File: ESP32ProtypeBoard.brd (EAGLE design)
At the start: 54.6 x 53.3 mm, 102 parts, among them IC2 SI4431BDY, J1 CONN_03_NO_SILK, J2 CONN_04_NO_SILK, J20 CONN_04_NO_SILK, J21 CONN_05_NO_SILK, J24 CONN_04_NO_SILK, J31 CONN_01_NO_SILK, J38 CONN_01_NO_SILK, J4 VCC_TERMINAL, J40 CONN_01_NO_SILK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

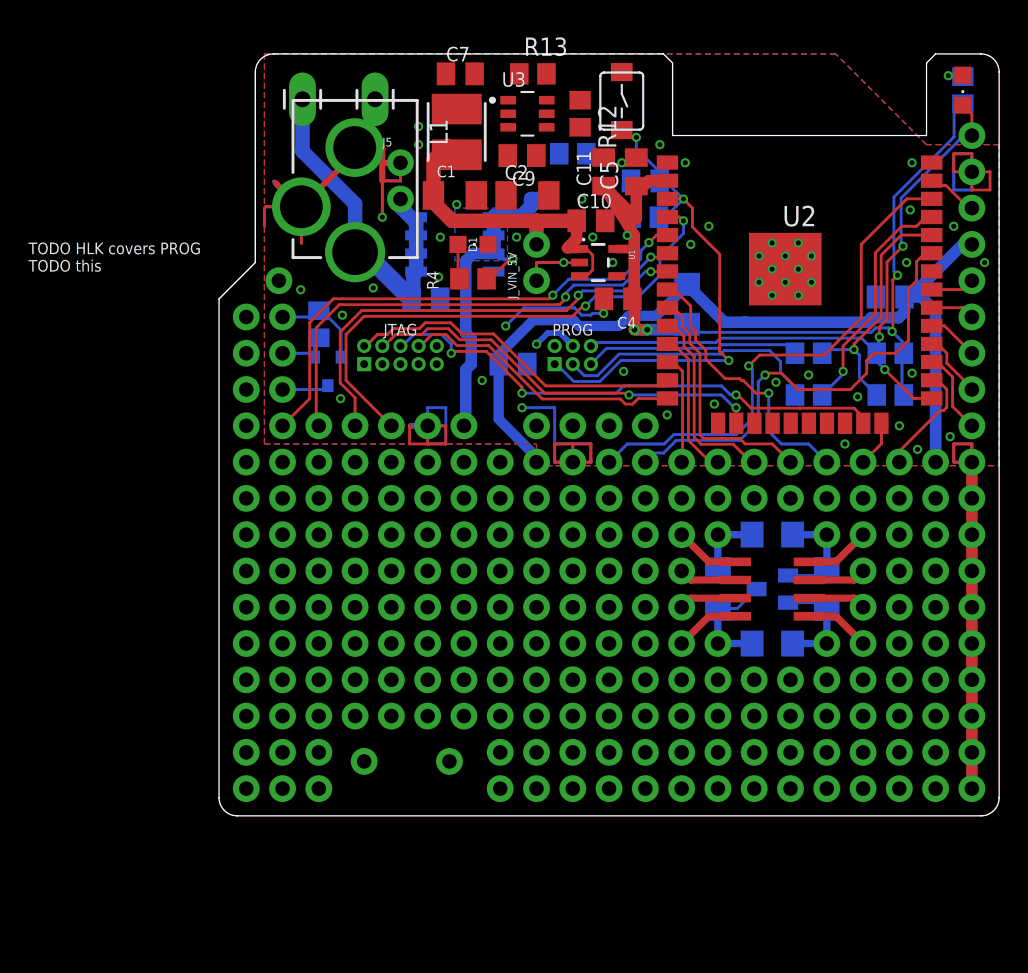
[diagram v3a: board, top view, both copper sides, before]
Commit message: Added custom modified DC-044 power jack
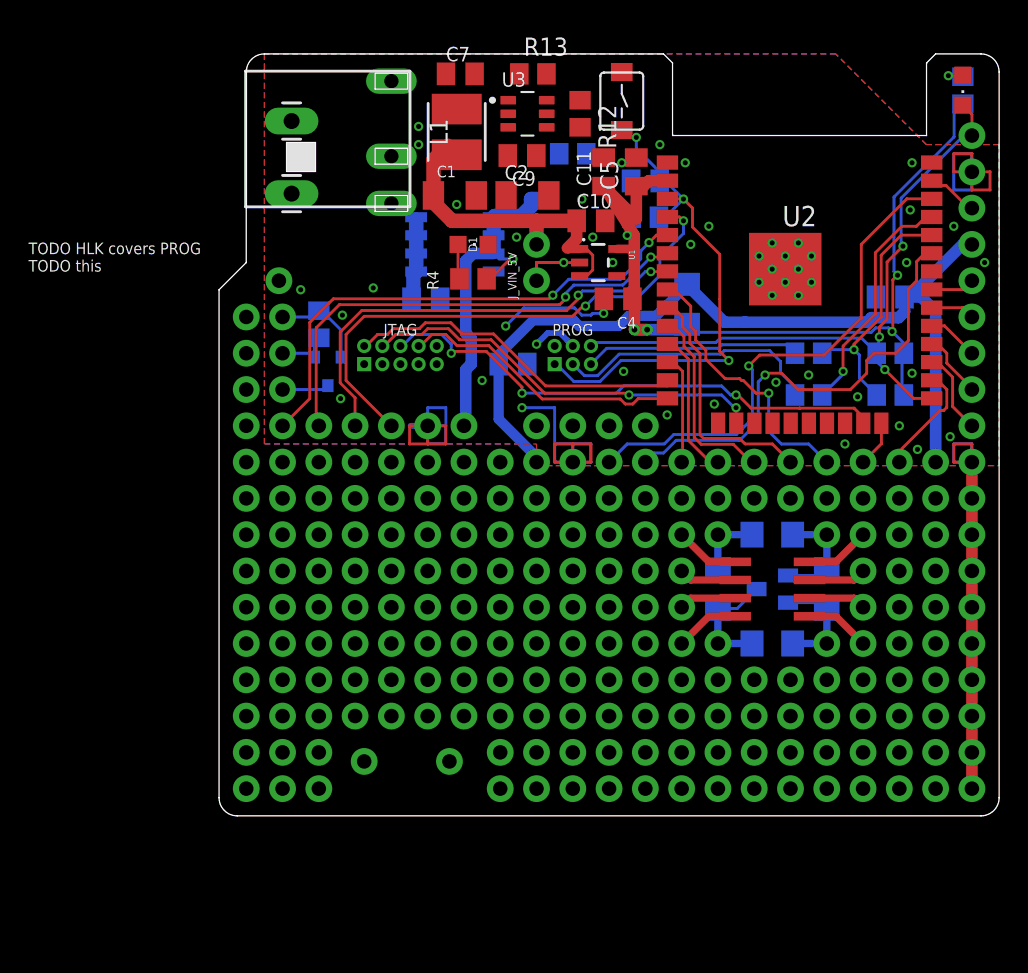
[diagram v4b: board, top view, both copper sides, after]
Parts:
- removed J37, J5: (no value), SparkFun-Connectors:1X01NS_KIT
- J10: value (none) -> DC-0440-2.5A-2.0; device SparkFun-Connectors:POWER_JACK_PTH_LOCK -> DC-0440-2.5A-2.0:DC044025A20
- moved J4 6.65 mm to (5.08, 43.6), turned to 90 degrees
- moved J3 6.04 mm to (5.08, 48.6), turned to 90 degrees
- moved J10 3.18 mm to (12.1, 51.4), turned to 0 degrees
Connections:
- net GND: now also J10.2, J10.3; no longer J10.GND, J10.GNDBREAK, J5.1
- net VCC: now also J10.1; no longer J10.PWR, J37.1
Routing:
- net GND: track 153.8 -> 111.1 mm, vias 41 -> 38
- net VCC: track 25.5 -> 5.85 mm
- removed copper zone on layer 16, net +12V
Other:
- outline, holes or cut-outs redrawn
- board text added: "7-17V"
- board text removed: "7-24V"

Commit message: WIP: new layout
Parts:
- moved C8 9.62 mm to (5.59, 39.9), flipped to the top
- moved IC2 5.18 mm to (11.4, 39.0), flipped to the top, turned to 180 degrees
- moved D1 0.51 mm to (18.3, 40.0)
- moved R4 0.51 mm to (18.3, 37.6)
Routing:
- net +12V: track 25.0 -> 13.9 mm, vias 1 -> 0
- net VCC: track 5.85 -> 2.54 mm
- net +5V: track 24.2 -> 21.2 mm
- net GND: vias 38 -> 34
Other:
- board text added: "Mikee © 2021/06 v3.1"
- board text removed: "Mikee © 2021/05 v3.1"
- board text removed: "TYA40124R7"

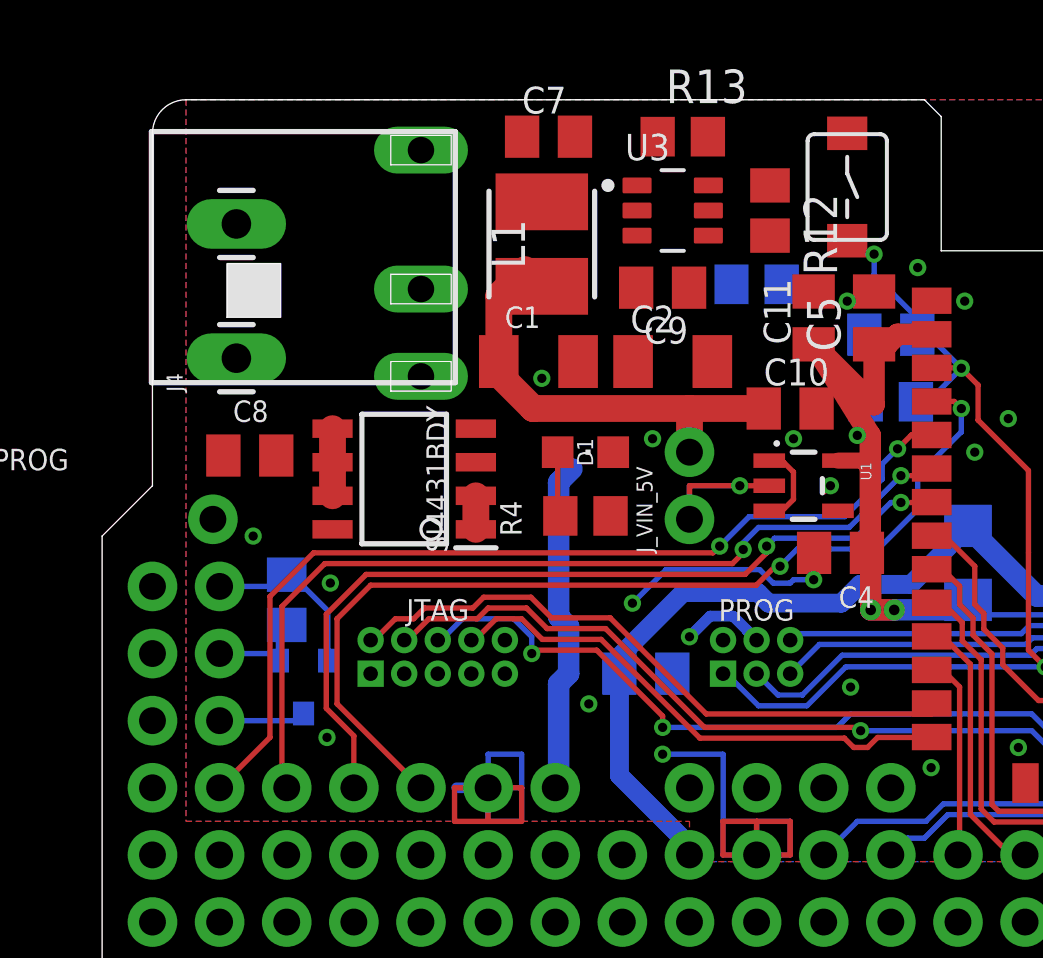
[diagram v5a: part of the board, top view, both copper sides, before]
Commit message: Wired new DCDC converter
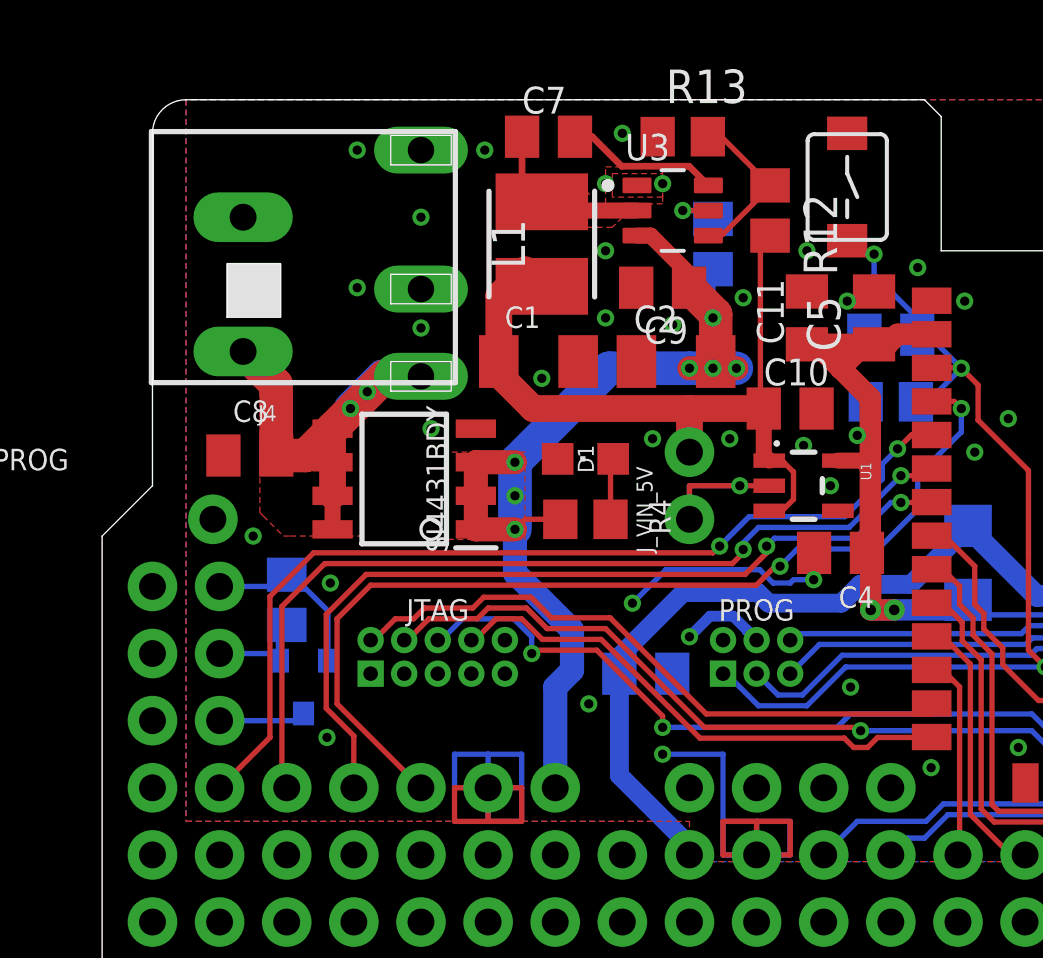
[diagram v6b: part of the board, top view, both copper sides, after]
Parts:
- J3: value (none) -> CONN_01_NO_SILK_LONGPAD; device SparkFun-Connectors:1X01_LONGPAD -> my-connectors:1X01_NO_SILK_LONGPAD
- J4: device SparkFun-Connectors:1X01_LONGPAD -> my-connectors:1X01_NO_SILK_LONGPAD
- moved R3 2.25 mm to (23.1, 47.9), turned to 90 degrees
- moved J3 0.36 mm to (5.33, 48.9), turned to 180 degrees
- moved J4 0.36 mm to (5.33, 43.8), turned to 180 degrees
- moved D1 0.25 mm to (18.3, 39.8), turned to 90 degrees
- moved C11 0.25 mm to (26.7, 45.1)
- moved C2 0.13 mm to (21.7, 43.4)
- moved R4 0.13 mm to (18.3, 37.5), turned to 0 degrees
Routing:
- net +12V: track 13.9 -> 41.1 mm, vias 0 -> 7
- net VCC: track 2.54 -> 18.2 mm, vias 0 -> 2
- net +5V: track 21.2 -> 29.5 mm
- net SW: track 0.00 -> 6.51 mm
- net VFB: track 0.00 -> 6.27 mm
- net VBST: track 0.00 -> 5.81 mm
- net VEN: track 0.00 -> 2.24 mm, vias 0 -> 1
- net GND: track 111.1 -> 112.0 mm, vias 34 -> 49
- net +3V3: track 64.6 -> 63.9 mm
- added copper zone on layer 1, net +12V
- added copper zone on layer 1, net SW
- added copper zone on layer 1, net VCC

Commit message: Layout tuning
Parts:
- moved J47 9.16 mm to (45.1, 24.8)
- moved J50 8.03 mm to (52.7, 27.3)
- moved J49 7.18 mm to (52.7, 29.8)
- moved J48 5.68 mm to (47.6, 24.8)
- moved C4 0.25 mm to (27.9, 35.9)
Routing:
- net IO4: track 7.93 -> 0.00 mm
- net IO16: track 5.87 -> 0.00 mm
- net IO17: track 4.60 -> 0.00 mm
- net IO2: track 3.25 -> 0.00 mm
- net GND: vias 49 -> 51

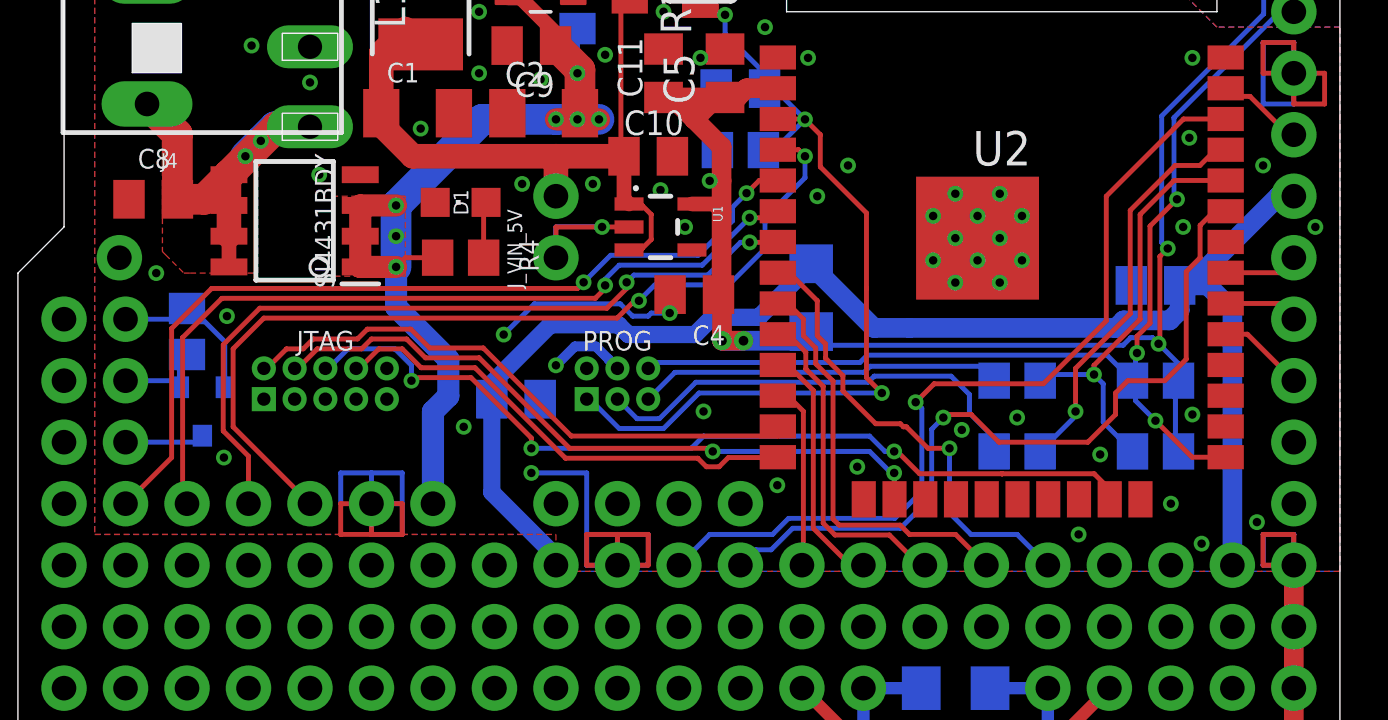
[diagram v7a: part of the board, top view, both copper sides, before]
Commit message: Connected moved pins, moved bottom silk
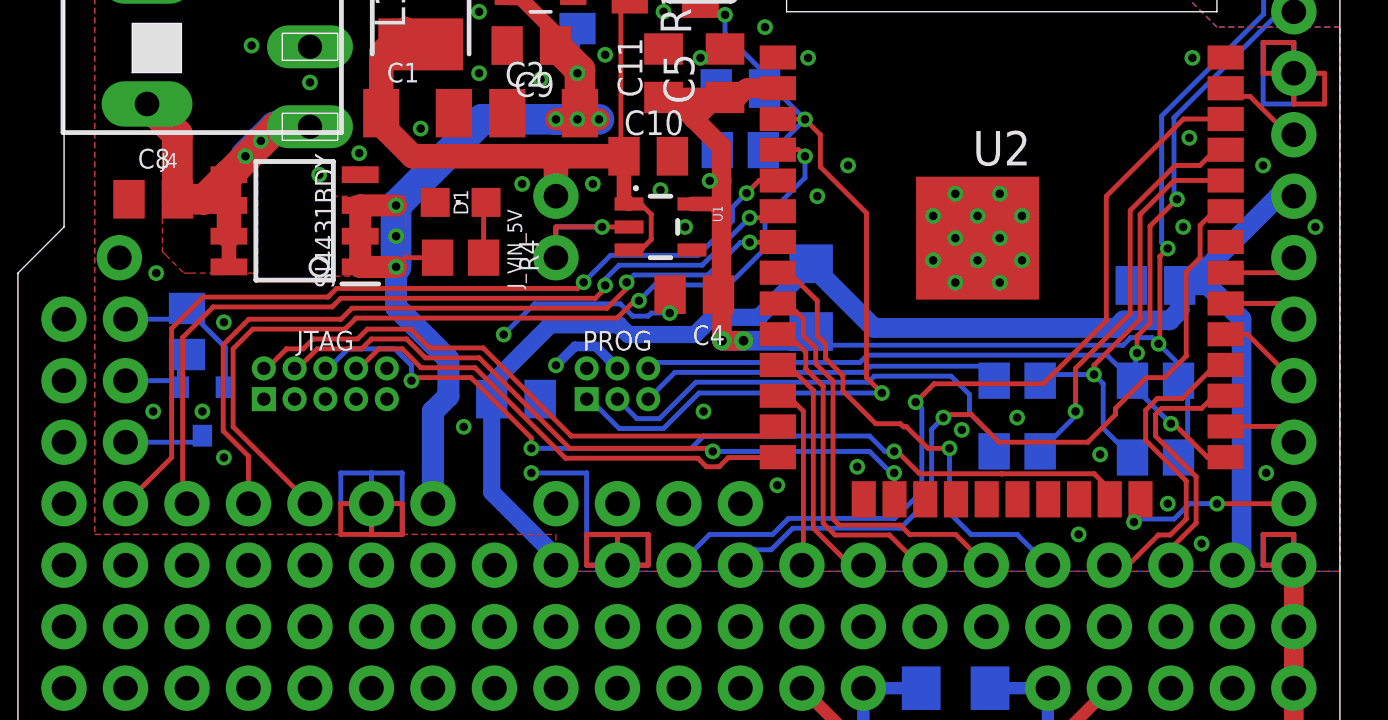
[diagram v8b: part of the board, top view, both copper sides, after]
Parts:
- moved R9 0.25 mm to (47.0, 29.2)
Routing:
- net IO17: track 0.00 -> 13.2 mm
- net IO16: track 0.00 -> 10.6 mm
- net IO2: track 0.00 -> 7.97 mm, vias 0 -> 2
- net IO4: track 0.00 -> 3.08 mm
- net GND: track 112.0 -> 113.4 mm, vias 51 -> 53
